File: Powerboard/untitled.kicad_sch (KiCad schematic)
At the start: 17 parts

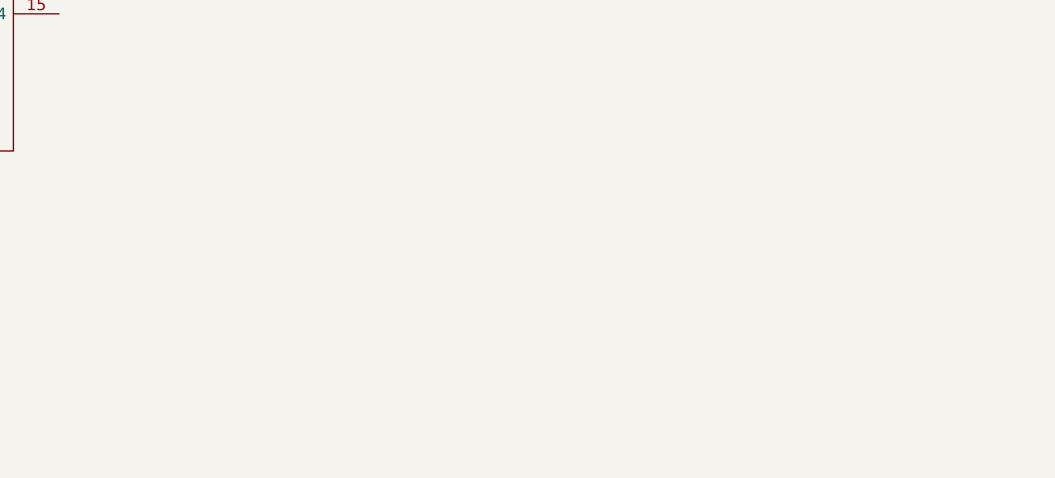
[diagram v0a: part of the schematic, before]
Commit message: added vbus to 3.3v converter
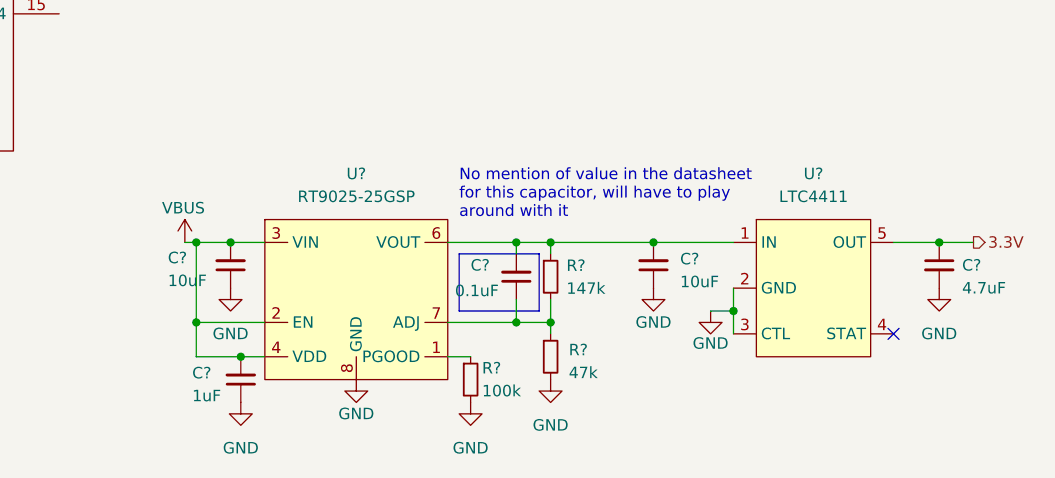
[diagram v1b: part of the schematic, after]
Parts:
- added C? (x2): 10uF, Capacitor_SMD:C_0603_1608Metric, symbol Device:C_Small
- added C?: 4.7uF, Capacitor_SMD:C_0603_1608Metric, symbol Device:C_Small
- added C?: 0.1uF, Capacitor_SMD:C_0603_1608Metric, symbol Device:C_Small
- added C?: 1uF, Capacitor_SMD:C_0603_1608Metric, symbol Device:C_Small
- added R?: 100k, Resistor_SMD:R_0603_1608Metric, symbol Device:R_Small
- added R?: 47k, Resistor_SMD:R_0603_1608Metric, symbol Device:R_Small
- added R?: 147k, Resistor_SMD:R_0603_1608Metric, symbol Device:R_Small
- added U?: RT9025-25GSP, Package_SO:SOP-8_3.9x4.9mm_P1.27mm, symbol iclr:RT9025-25GSP
- added U?: LTC4411, Package_TO_SOT_SMD:SOT-23-5, symbol iclr:LTC4411
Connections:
- net GND: now also C?.1, C?.1, C?.1, C?.2, R?.2, R?.2, U?.2 (GND), U?.3 (CTL), U?.8 (GND)
- net VBUS: now also C?.2, C?.2, U?.2 (EN), U?.3 (VIN), U?.4 (VDD)
- new net: R?.1, U?.1 (PGOOD)
- new net: C?.2, C?.2, R?.1, U?.1 (IN), U?.6 (VOUT)
- new net: C?.1, R?.1, R?.2, U?.7 (ADJ)
- new net 3.3V: C?.1, U?.5 (OUT)
- no-connect marks 19 -> 20
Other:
- note added: "No mention of value in the datasheet for this capacitor, will have to play around with it"
